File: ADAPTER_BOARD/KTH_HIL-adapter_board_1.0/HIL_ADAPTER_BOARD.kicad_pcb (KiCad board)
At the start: 2 copper layers, 95 x 85 mm, 33 parts, among them CN10 Conn_02x20_Odd_Even, CN11 Conn_02x36_Odd_Even, CN12 Conn_02x36_Odd_Even, CN7 Conn_02x20_Odd_Even, U1 SN65HVD233, U2 SN65HVD233

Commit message: fixed timer issue in routing
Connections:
- CN11 pad 37: /595_Enable -> Net-(CN11-Pad37)
- CN12 pad 52: Net-(CN12-Pad52) -> /595_Enable
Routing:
- net /595_Enable: track 19.2 -> 101.9 mm, vias 1 -> 5

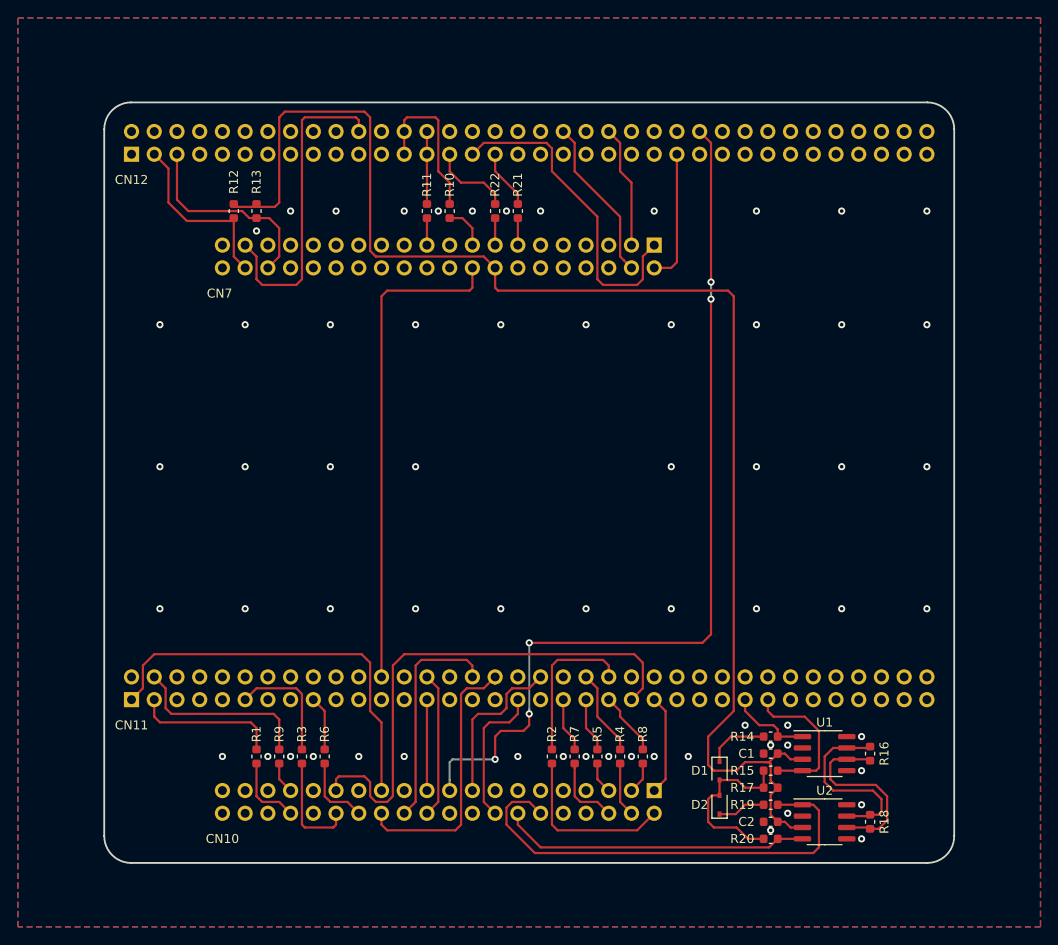
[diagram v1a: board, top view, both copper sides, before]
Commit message: Fixed comments regarding schematic
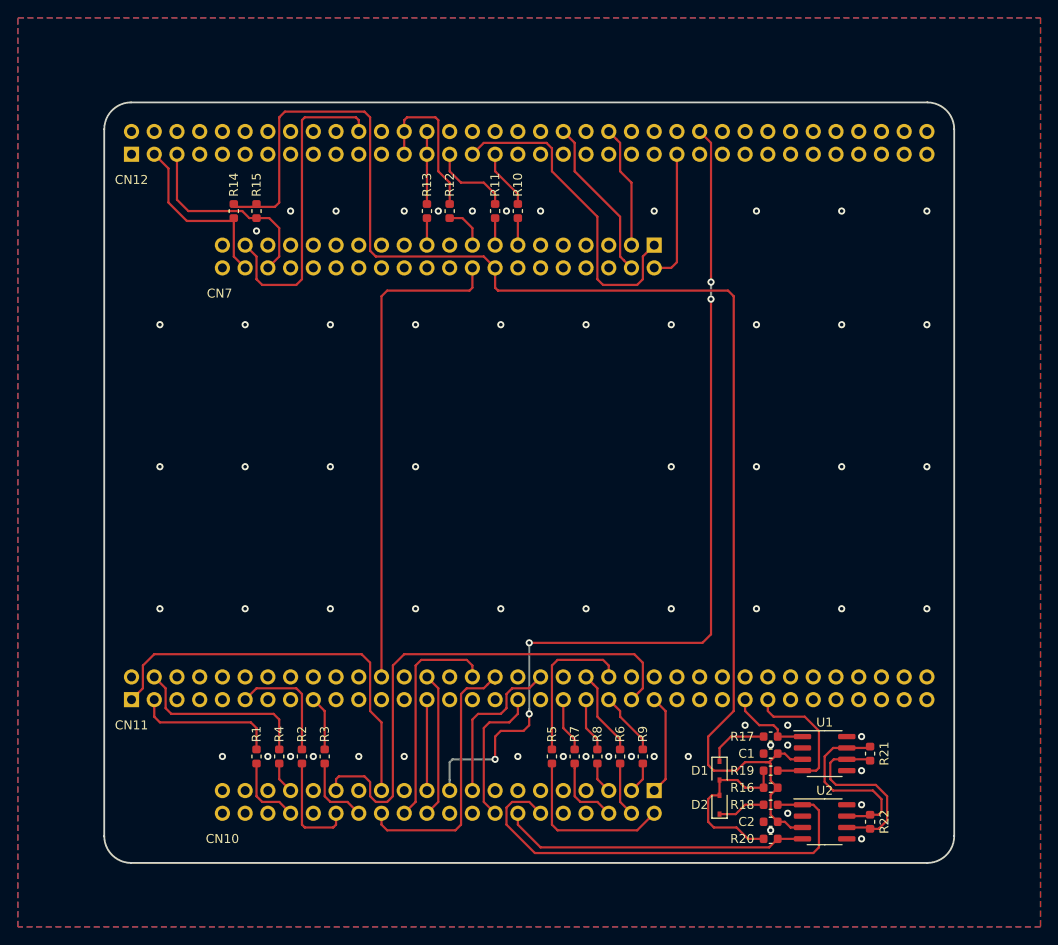
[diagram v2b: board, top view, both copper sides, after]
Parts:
- renumbered R21 to R10, R22 to R11, R10 to R12, R11 to R13, R12 to R14, R13 to R15, R17 to R16, R14 to R17, R19 to R18, R15 to R19, R3 to R2, R16 to R21, R18 to R22, R6 to R3, R9 to R4, R2 to R5, R4 to R6, R5 to R8, R8 to R9
